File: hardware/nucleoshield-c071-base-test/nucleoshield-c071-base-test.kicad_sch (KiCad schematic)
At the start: 13 parts, among them J1 Power, J2 Digital/PWM, J3 Analog, J4 Digital/PWM, J5 Conn_02x03_Odd_Even

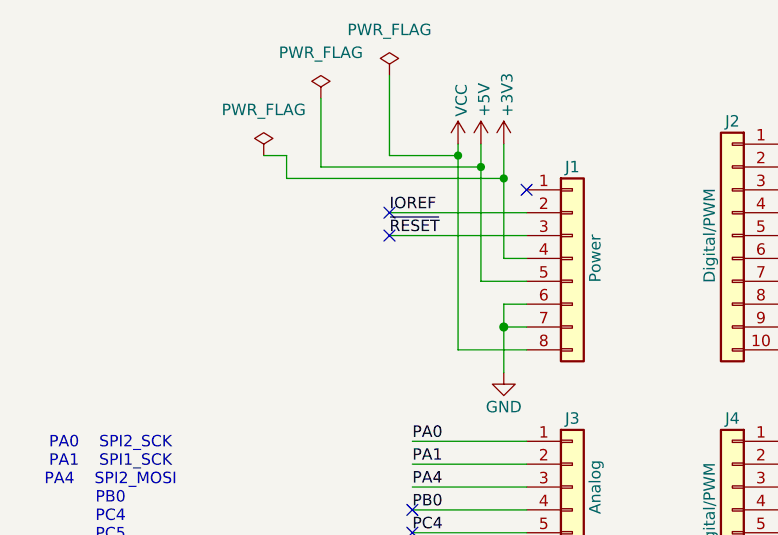
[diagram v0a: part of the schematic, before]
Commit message: added nucleoshield template
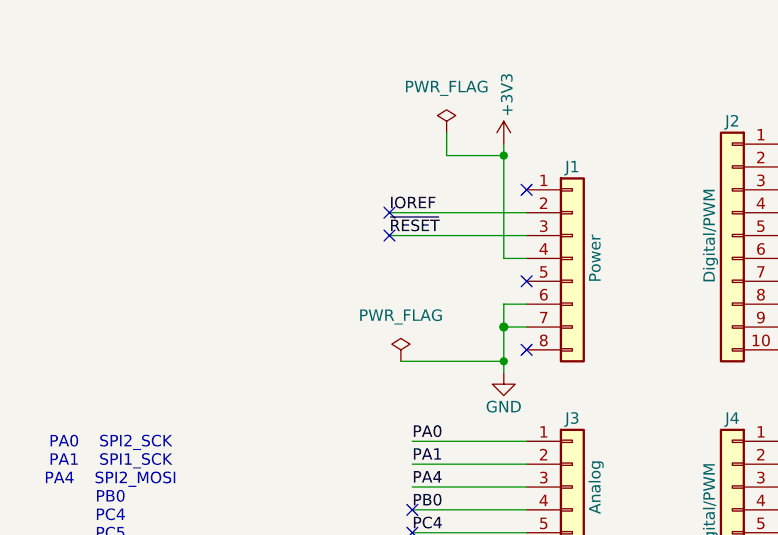
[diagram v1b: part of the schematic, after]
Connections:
- net +5V: no longer names the net of J1.5 (Pin_5)
- net VCC: no longer names the net of J1.8 (Pin_8)
- no-connect marks 22 -> 24
